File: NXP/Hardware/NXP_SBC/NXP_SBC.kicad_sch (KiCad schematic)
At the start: 0 parts

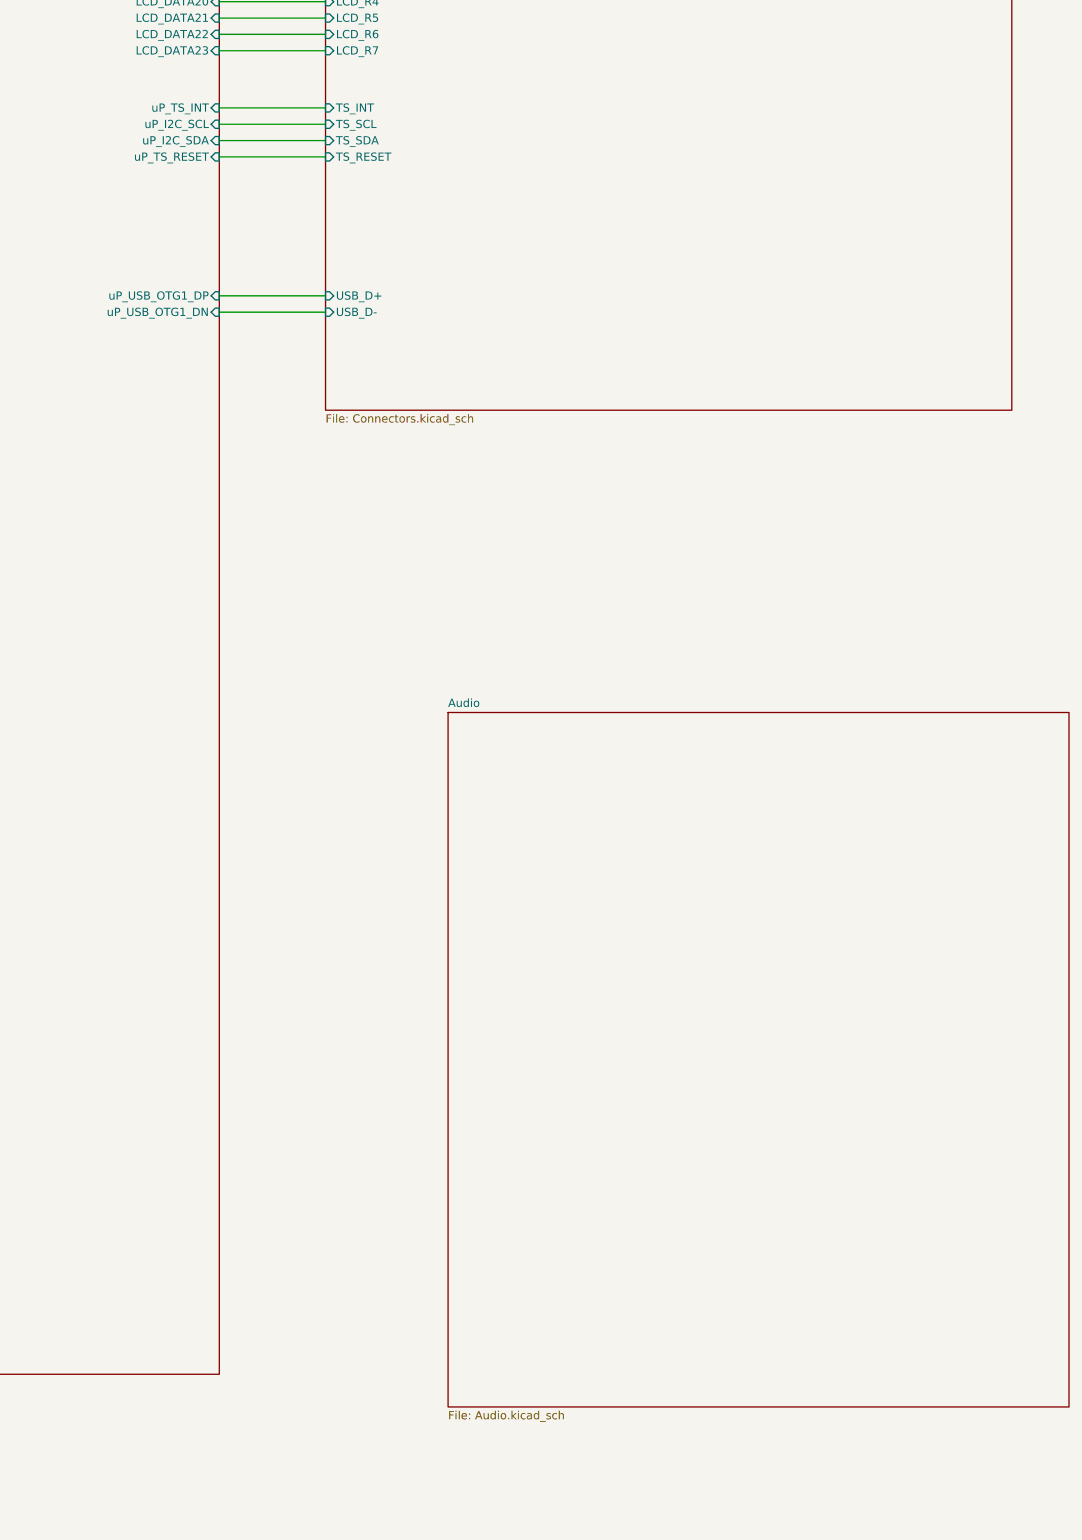
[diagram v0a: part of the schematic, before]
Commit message: Finished audio section
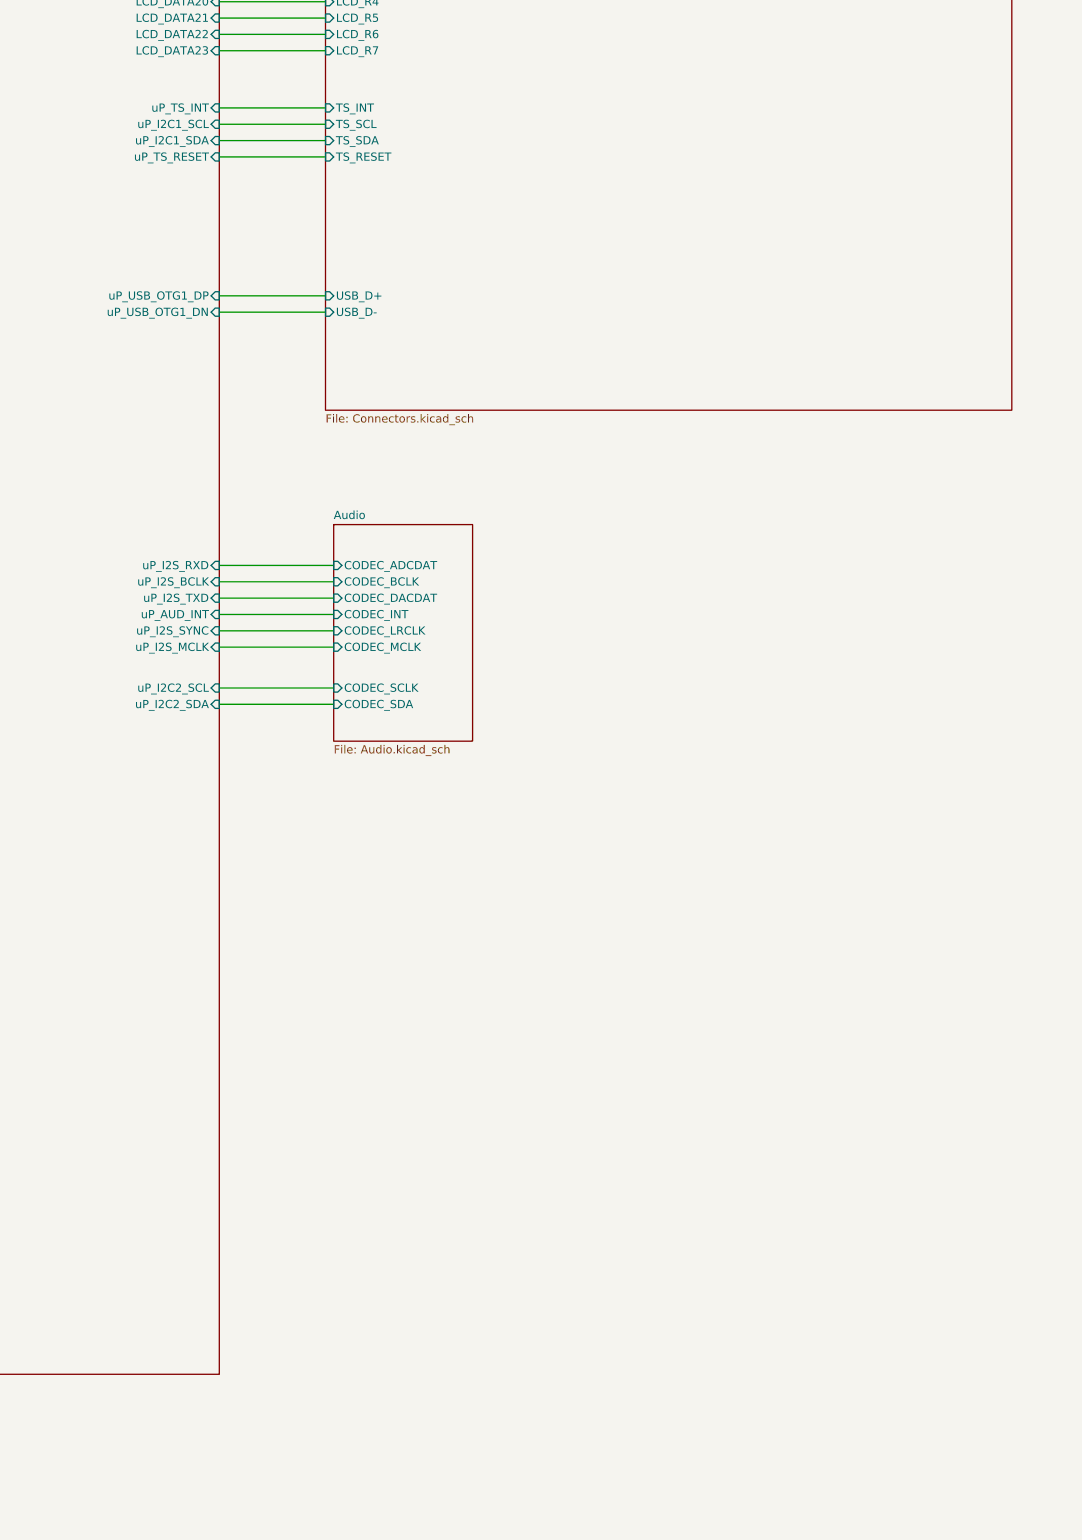
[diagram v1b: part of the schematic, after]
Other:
- sheet Audio ports: added CODEC_ADCDAT, CODEC_BCLK, CODEC_DACDAT, CODEC_INT, CODEC_LRCLK, CODEC_MCLK, CODEC_SCLK, CODEC_SDA; removed none
- sheet Processor ports: added uP_AUD_INT, uP_I2C1_SCL, uP_I2C1_SDA, uP_I2C2_SCL, uP_I2C2_SDA, uP_I2S_BCLK, uP_I2S_MCLK, uP_I2S_RXD, uP_I2S_SYNC, uP_I2S_TXD; removed uP_I2C_SCL, uP_I2C_SDA
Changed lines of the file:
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@@
 	(wire
 		(pts
+			(xy 495.3 318.77) (xy 513.08 318.77)
+		)
+		(stroke
+			(width 0)
+			(type default)
+		)
+	)
+	(wire
+		(pts
 			(xy 355.6 191.77) (xy 386.08 191.77)
 		)
@@
 	(wire
 		(pts
+			(xy 495.3 321.31) (xy 513.08 321.31)
+		)
+		(stroke
+			(width 0)
+			(type default)
+		)
+	)
+	(wire
+		(pts
 			(xy 495.3 161.29) (xy 511.81 161.29)
 		)
@@
 	(wire
 		(pts
+			(xy 495.3 309.88) (xy 513.08 309.88)
+		)
+		(stroke
+			(width 0)
+			(type default)
+		)
+	)
+	(wire
+		(pts
 			(xy 355.6 264.16) (xy 386.08 264.16)
 		)
@@
 	(wire
 		(pts
+			(xy 495.3 302.26) (xy 513.08 302.26)
+		)
+		(stroke
+			(width 0)
+			(type default)
+		)
+	)
+	(wire
+		(pts
 			(xy 495.3 176.53) (xy 511.81 176.53)
 		)
@@
 	(wire
 		(pts
+			(xy 495.3 304.8) (xy 513.08 304.8)
+		)
+		(stroke
+			(width 0)
+			(type default)
+		)
+	)
+	(wire
+		(pts
+			(xy 495.3 307.34) (xy 513.08 307.34)
+		)
+		(stroke
+			(width 0)
+			(type default)
+		)
+	)
+	(wire
+		(pts
 			(xy 495.3 163.83) (xy 511.81 163.83)
 		)
@@
 	(wire
 		(pts
+			(xy 495.3 299.72) (xy 513.08 299.72)
+		)
+		(stroke
+			(width 0)
+			(type default)
+		)
+	)
+	(wire
+		(pts
 			(xy 354.33 157.48) (xy 386.08 157.48)
 		)
@@
 	(wire
 		(pts
+			(xy 495.3 312.42) (xy 513.08 312.42)
+		)
+		(stroke
+			(width 0)
+			(type default)
+		)
+	)
+	(wire
+		(pts
 			(xy 495.3 257.81) (xy 511.81 257.81)
 		)
@@
 			)
 		)
-		(pin "uP_I2C_SCL" input
-			(at 495.3 231.14 0)
+		(pin "uP_USB_OTG1_DN" input
+			(at 495.3 260.35 0)
 			(effects
 				(font
@@
 			)
 		)
-		(pin "uP_I2C_SDA" input
-			(at 495.3 233.68 0)
+		(pin "uP_USB_OTG1_DP" input
+			(at 495.3 257.81 0)
 			(effects
 				(font
@@
 			)
 		)
-		(pin "uP_USB_OTG1_DN" input
-			(at 495.3 260.35 0)
+		(pin "uP_LCD_DISP" input
+			(at 495.3 140.97 0)
 			(effects
 				(font
@@
 			)
 		)
-		(pin "uP_USB_OTG1_DP" input
-			(at 495.3 257.81 0)
+		(pin "uP_TS_INT" input
+			(at 495.3 228.6 0)
 			(effects
 				(font
@@
 			)
 		)
-		(pin "uP_LCD_DISP" input
-			(at 495.3 140.97 0)
+		(pin "uP_TS_RESET" input
+			(at 495.3 236.22 0)
 			(effects
 				(font
@@
 			)
 		)
-		(pin "uP_TS_INT" input
-			(at 495.3 228.6 0)
+		(pin "uP_I2S_MCLK" input
+			(at 495.3 312.42 0)
 			(effects
 				(font
@@
 			)
 		)
-		(pin "uP_TS_RESET" input
-			(at 495.3 236.22 0)
+		(pin "uP_AUD_INT" input
+			(at 495.3 307.34 0)
+			(effects
+				(font
+					(size 1.27 1.27)
+				)
+				(justify right)
+			)
+		)
+		(pin "uP_I2S_TXD" input
+			(at 495.3 304.8 0)
+			(effects
+				(font
+					(size 1.27 1.27)
+				)
+				(justify right)
+			)
+		)
+		(pin "uP_I2S_RXD" input
+			(at 495.3 299.72 0)
+			(effects
+				(font
+					(size 1.27 1.27)
+				)
+				(justify right)
+			)
+		)
+		(pin "uP_I2S_BCLK" input
+			(at 495.3 302.26 0)
+			(effects
+				(font
+					(size 1.27 1.27)
+				)
+				(justify right)
+			)
+		)
+		(pin "uP_I2C2_SCL" input
+			(at 495.3 318.77 0)
+			(effects
+				(font
+					(size 1.27 1.27)
+				)
+				(justify right)
+			)
+		)
+		(pin "uP_I2S_SYNC" input
+			(at 495.3 309.88 0)
+			(effects
+				(font
+					(size 1.27 1.27)
+				)
+				(justify right)
+			)
+		)
+		(pin "uP_I2C2_SDA" input
+			(at 495.3 321.31 0)
+			(effects
+				(font
+					(size 1.27 1.27)
+				)
+				(justify right)
+			)
+		)
+		(pin "uP_I2C1_SCL" input
+			(at 495.3 231.14 0)
+			(effects
+				(font
+					(size 1.27 1.27)
+				)
+				(justify right)
+			)
+		)
+		(pin "uP_I2C1_SDA" input
+			(at 495.3 233.68 0)
 			(effects
 				(font
@@
 	)
 	(sheet
-		(at 530.86 322.58)
-		(size 96.52 107.95)
+		(at 513.08 293.37)
+		(size 21.59 33.655)
 		(exclude_from_sim no)
 		(in_bom yes)
@@
 		)
 		(property "Sheetname" "Audio"
-			(at 530.86 321.8684 0)
+			(at 513.08 292.6584 0)
 			(effects
 				(font
@@
 		)
 		(property "Sheetfile" "Audio.kicad_sch"
-			(at 530.86 431.1146 0)
+			(at 513.08 327.6096 0)
 			(effects
 				(font
@@
 			)
 		)
+		(pin "CODEC_ADCDAT" input
+			(at 513.08 299.72 180)
+			(effects
+				(font
+					(size 1.27 1.27)
+				)
+				(justify left)
+			)
+		)
+		(pin "CODEC_BCLK" input
+			(at 513.08 302.26 180)
+			(effects
+				(font
+					(size 1.27 1.27)
+				)
+				(justify left)
+			)
+		)
+		(pin "CODEC_DACDAT" input
+			(at 513.08 304.8 180)
+			(effects
+				(font
+					(size 1.27 1.27)
+				)
+				(justify left)
+			)
+		)
+		(pin "CODEC_INT" input
+			(at 513.08 307.34 180)
+			(effects
+				(font
+					(size 1.27 1.27)
+				)
+				(justify left)
+			)
+		)
+		(pin "CODEC_LRCLK" input
+			(at 513.08 309.88 180)
+			(effects
+				(font
+					(size 1.27 1.27)
+				)
+				(justify left)
+			)
+		)
+		(pin "CODEC_MCLK" input
+			(at 513.08 312.42 180)
+			(effects
+				(font
+					(size 1.27 1.27)
+				)
+				(justify left)
+			)
+		)
+		(pin "CODEC_SCLK" input
+			(at 513.08 318.77 180)
+			(effects
+				(font
+					(size 1.27 1.27)
+				)
+				(justify left)
+			)
+		)
+		(pin "CODEC_SDA" input
+			(at 513.08 321.31 180)
+			(effects
+				(font
+					(size 1.27 1.27)
+				)
+				(justify left)
+			)
+		)

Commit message: Updates to radio connections
Also used the pin configurator tool to better understand pin mapping of the imx processor
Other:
- sheet Processor ports: added RADIO_SD_CLK, RADIO_SD_CMD, RADIO_SD_DATA0, RADIO_SD_DATA1, RADIO_SD_DATA2, RADIO_SD_DATA3, uP_GPIO4_IO0, uP_GPIO4_IO1, uP_GPIO4_IO2, uP_GPIO4_IO3, uP_SAI1_MCLK, uP_SAI1_RX_DATA, uP_SAI1_TX_BCLK, uP_SAI1_TX_DATA, uP_SAI1_TX_SYNC, uP_UART1_CTS_B, uP_UART1_RTS_B, uP_UART1_RX_DATA, uP_UART1_TX_DATA, uP_UART2_CTS_B, uP_UART2_RTS_B, uP_UART2_RX_DATA, uP_UART2_TX_DATA; removed none
- sheet Radio ports: added RADIO_BT_15.4_DEV_WAKE, RADIO_BT_15.4_WAKE__HOST, RADIO_EXT_GNT/SPI_RX, RADIO_EXT_PRI/SPI_TX, RADIO_EXT_STATE/SPI_CLK, RADIO_JTAG_TDI, RADIO_JTAG_TDO, RADIO_JTAG_TMS, RADIO_PCM_CLK, RADIO_PCM_DIN, RADIO_PCM_DOUT, RADIO_PCM_MCLK, RADIO_PCM_SYNC, RADIO_PDN, RADIO_RF_ANT0, RADIO_RF_CNTL0, RADIO_RF_CNTL2, RADIO_RF_CNTL3, RADIO_RF_CNTL4, RADIO_RST_IND, RADIO_SD_CLK, RADIO_SD_CMD, RADIO_SD_DAT[0], RADIO_SD_DAT[1], RADIO_SD_DAT[2], RADIO_SD_DAT[3], RADIO_SD_INT, RADIO_UART_CTS, RADIO_UART_RTS, RADIO_UART_RX, RADIO_UART_TX, RADIO_WCI_SIN, RADIO_WCI_SOUT, RADIO_WL_DEV_WAKE, RADIO_WL_WAKE_HOST; removed none

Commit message: minor updates
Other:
- sheet Processor ports: added uP_GPIO4_IO10, uP_GPIO4_IO11, uP_GPIO4_IO12, uP_GPIO4_IO15, uP_GPIO4_IO6, uP_GPIO4_IO7, uP_GPIO4_IO8, uP_GPIO4_IO9, uP_SD2_CLK, uP_SD2_CMD, uP_SD2_DATA0, uP_SD2_DATA1, uP_SD2_DATA2, uP_SD2_DATA3; removed RADIO_SD_CLK, RADIO_SD_CMD, RADIO_SD_DATA0, RADIO_SD_DATA1, RADIO_SD_DATA2, RADIO_SD_DATA3, uP_GPIO4_IO0, uP_GPIO4_IO1, uP_GPIO4_IO2, uP_GPIO4_IO3
- sheet Radio ports: added RADIO_BT_15.4_RST, RADIO_WL_RST; removed RADIO_EXT_GNT/SPI_RX, RADIO_EXT_PRI/SPI_TX, RADIO_EXT_STATE/SPI_CLK, RADIO_JTAG_TDI, RADIO_JTAG_TDO, RADIO_JTAG_TMS, RADIO_RF_ANT0, RADIO_RF_CNTL0, RADIO_RF_CNTL2, RADIO_RF_CNTL3, RADIO_RF_CNTL4, RADIO_WCI_SIN, RADIO_WCI_SOUT
